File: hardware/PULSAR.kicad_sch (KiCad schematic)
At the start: 8 parts, among them J1 Conn_01x20, J2 Conn_01x04, U1 AP2112K-3.3, U2 SS49E, U3 CD74HC4067M, U4 ADS8688

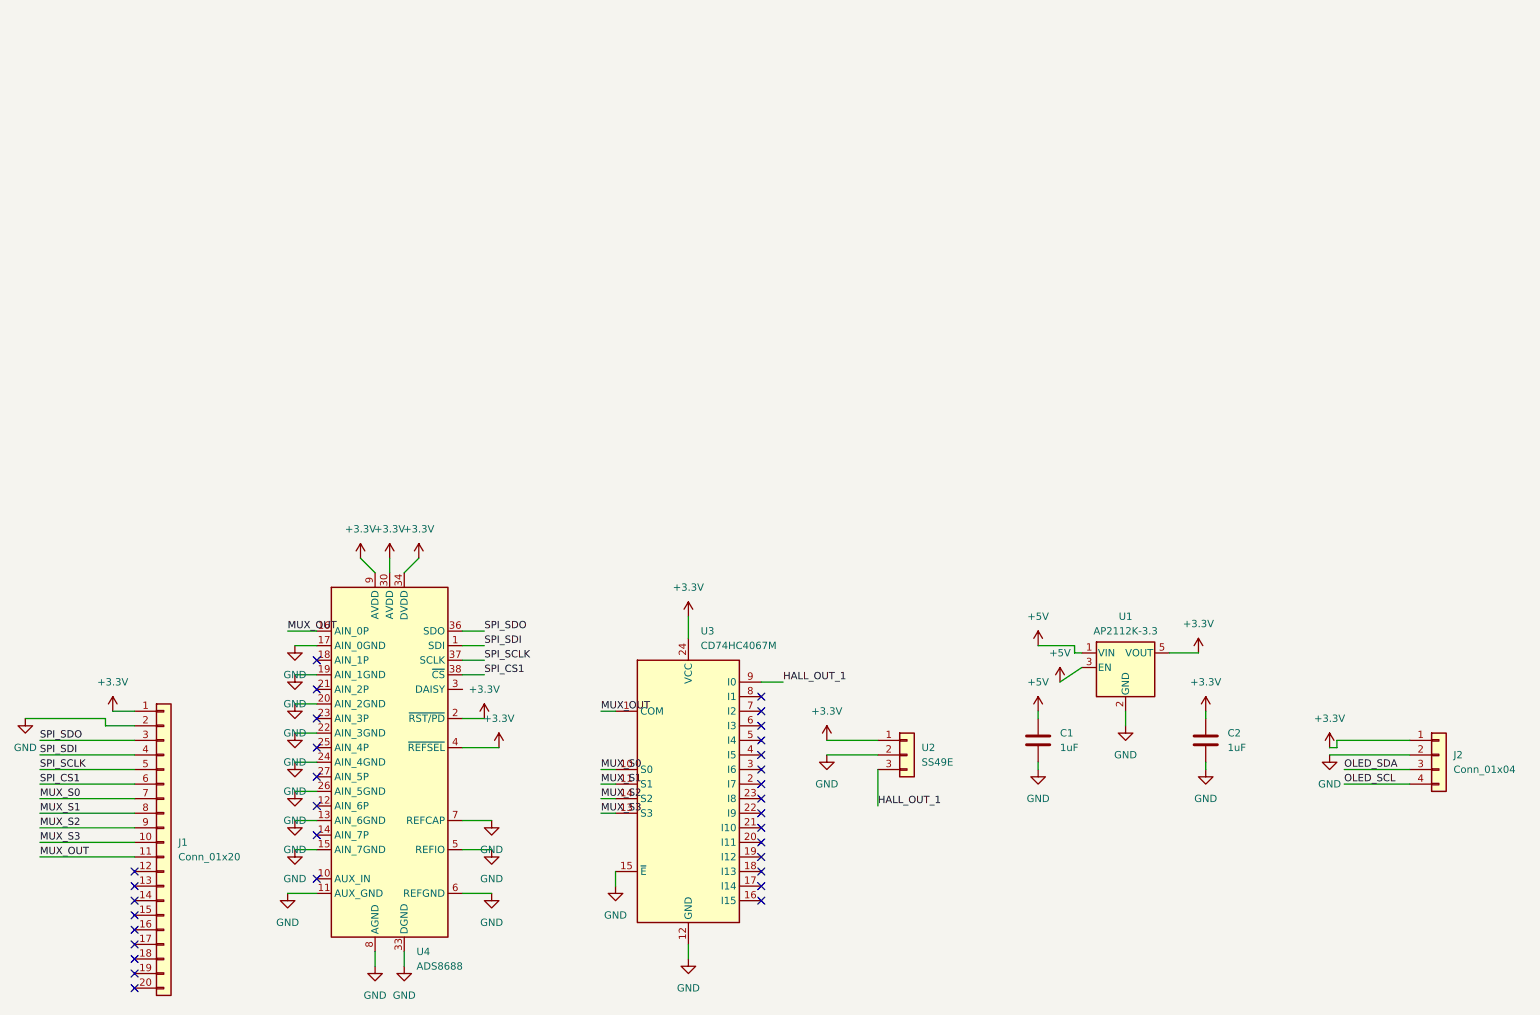
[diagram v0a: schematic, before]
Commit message: Kicad (#6)
* feat: add power section schematic AP2112K-3.3 LDO 5V to 3.3V

* feat: add Hall sensor SS49E schematic with HALL_OUT_1 net

* feat: add MUX CD74HC4067M schematic with control signals

* feat: add ADS8688 ADC schematic with SPI signals and analog input from MUX

* feat: add OrangeCrab connector with SPI, MUX and power signals

* feat: add OLED SSD1306 connector with SPI signals

* feat: add USB-C connector with power and data signals

* fix: resolve ERC errors, add PWR_FLAG and DAISY no-connect

* feat: assign footprints to all schematic components

* feat: setup 4-layer PCB and import schematic footprints

* feat: initial PCB layout component placement

* feat: complete PCB routing and fix DRC errors

* feat: generate gerber files for JLCPCB manufacturing

* feat: generate gerber files for JLCPCB manufacturing

---------

Co-authored-by: Emiliano <elmemiesenano@gmail.com>
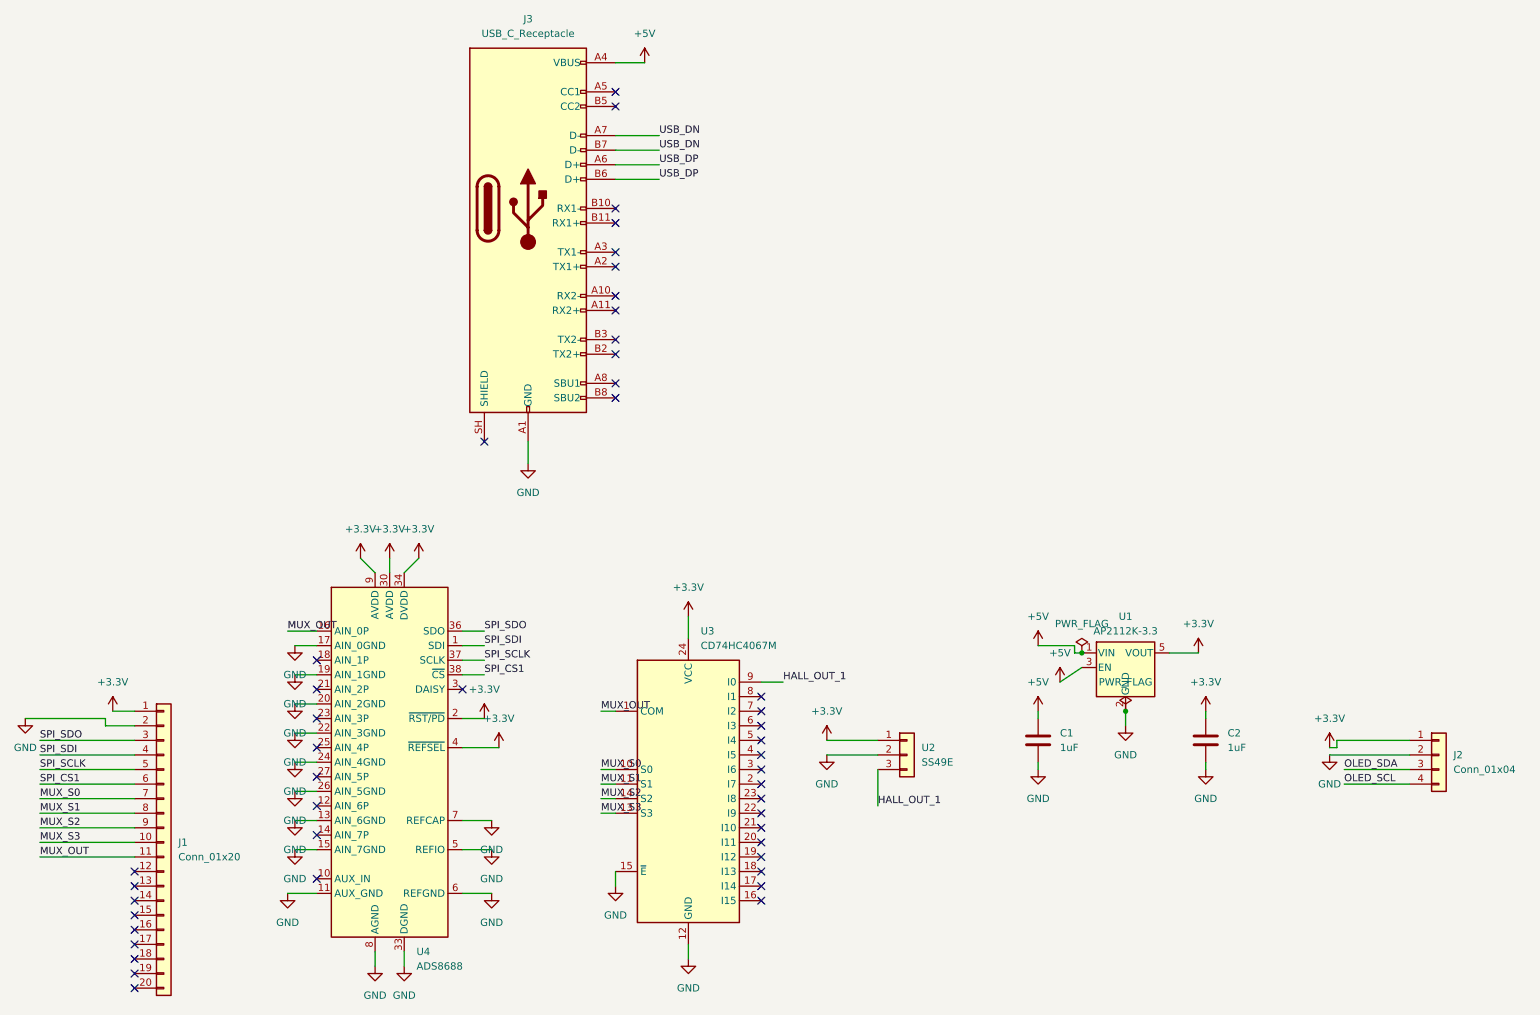
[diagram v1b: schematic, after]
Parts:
- added J3: USB_C_Receptacle, Connector_USB:USB_C_Receptacle_GCT_USB4115-03-C, symbol Connector:USB_C_Receptacle
- C1, C2: footprint (none) -> Capacitor_SMD:C_0805_2012Metric
- J1: footprint (none) -> Connector_PinHeader_2.54mm:PinHeader_1x20_P2.54mm_Vertical
- J2: footprint (none) -> Connector_PinHeader_2.54mm:PinHeader_1x04_P2.54mm_Vertical
- U2: footprint (none) -> Package_TO_SOT_THT:TO-92_Inline
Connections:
- net +5V: now also J3.A4 (VBUS), J3.A9 (VBUS), J3.B4 (VBUS), J3.B9 (VBUS)
- net GND: now also J3.A1 (GND), J3.A12 (GND), J3.B1 (GND), J3.B12 (GND)
- new net USB_DN: J3.A7 (D-), J3.B7 (D-)
- new net USB_DP: J3.A6 (D+), J3.B6 (D+)
- no-connect marks 32 -> 46
